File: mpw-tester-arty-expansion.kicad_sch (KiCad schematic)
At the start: 119 parts, among them J1 USB4105-GF-A, J10 61300211121, J11 61300211121, J12 61300211121, J14 61300311121, J15 61300311121, J18 61300411121, J19 61300711121, J2 61300211121, J20 61300411121, J3 Arty_A7_SPI, J4 61300211121, J5 61300311121, J6 61300211121, J7 61300211121, J8 61300211121, J9 61300211121, Q1 DTC014TEBTL, U1 SN74LVC1G125DCKR, U2 FT232HQ, U3 SN74LVC1G125DCKR, U4 MAX811REUS+T, U5 NTS0102DP, U6 MCP4661-103E/ML, U7 Caravel_breakout_PCB, U8 W25Q32FVSS, U9 MIC2211-AAYML-TR, Y1 ABM8G-12.000MHZ-18-D2Y-T, Y2 ECS-2520MVLC-100-BN-TR

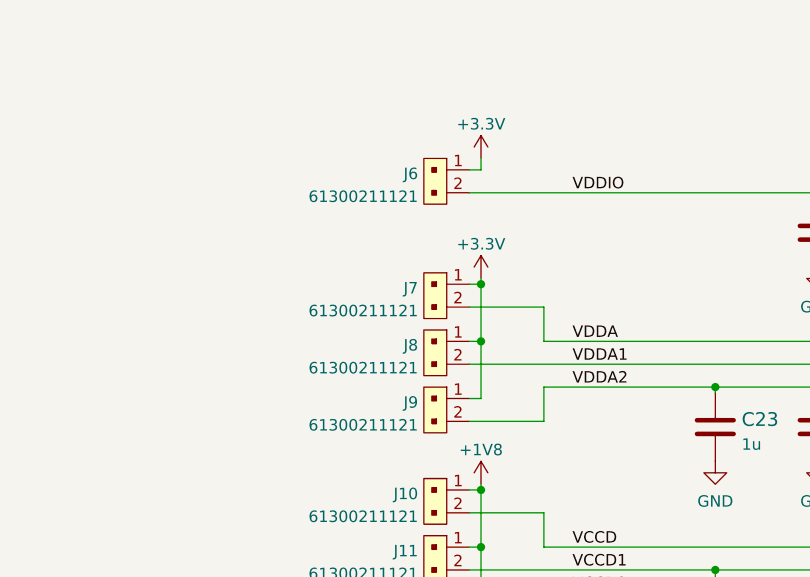
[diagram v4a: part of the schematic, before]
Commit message: Start power section layout. Adjust J6-J12 position on schematic to resolve crosses on PCB
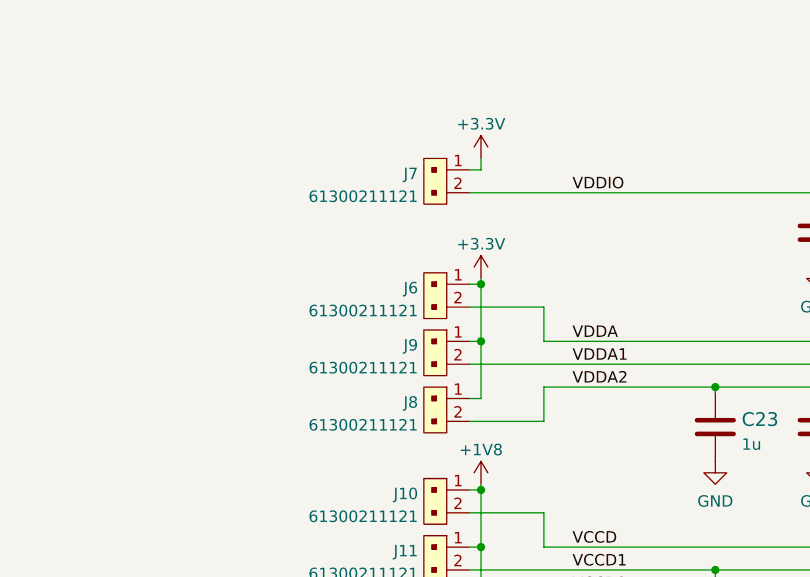
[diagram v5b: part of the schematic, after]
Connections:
- net VDDA: now also J6.2; no longer J7.2
- net VDDA1: now also J9.2; no longer J8.2
- net VDDA2: now also J8.2; no longer J9.2
- net VDDIO: now also J7.2; no longer J6.2
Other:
- moved on the sheet: J6, J7, J8, J9
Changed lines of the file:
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@@
     (rev "0.0.99")
   )
-  (bus_alias "SPI_FLASH" (members "~{CS}" "SCK" "SI" "SO" "~{WP}" "~{HOLD}"))
   (bus_alias "SPI" (members "~{CS}" "MISO" "MOSI" "SCK"))
+  (bus_alias "SPI_FLASH" (members "~{CS}" "SCK" "SI" "SO" "~{WP}" "~{HOLD}"))
   (junction (at 122.555 74.93) (diameter 0) (color 0 0 0 0)
   )
@@
     (pin "8")
   )
-  (symbol (lib_id "antmicroRectangularConnectorsHeadersMalePins:61300211121") (at 305.435 182.245 270) (unit 1)
+  (symbol (lib_id "antmicroRectangularConnectorsHeadersMalePins:61300211121") (at 305.435 169.545 270) (unit 1)
     (in_bom yes) (on_board yes) (fields_autoplaced)
-    (property "Reference" "J7" (id 0) (at 302.26 182.6803 90)
+    (property "Reference" "J7" (id 0) (at 302.26 169.9803 90)
       (effects (font (size 1.27 1.27)) (justify right))
     )
-    (property "Value" "61300211121" (id 1) (at 302.26 185.2172 90)
+    (property "Value" "61300211121" (id 1) (at 302.26 172.5172 90)
       (effects (font (size 1.27 1.27)) (justify right))
     )
-    (property "Footprint" "antmicro-footprints:PinHeader_1x2_P2.54_Drill0.9mm" (id 2) (at 310.515 187.325 0)
+    (property "Footprint" "antmicro-footprints:PinHeader_1x2_P2.54_Drill0.9mm" (id 2) (at 310.515 174.625 0)
       (effects (font (size 1.524 1.524)) (justify left) hide)
     )
-    (property "Datasheet" "https://katalog.we-online.de/em/datasheet/6130xx11121.pdf" (id 3) (at 313.055 187.325 0)
+    (property "Datasheet" "https://katalog.we-online.de/em/datasheet/6130xx11121.pdf" (id 3) (at 313.055 174.625 0)
       (effects (font (size 1.524 1.524)) (justify left) hide)
     )
-    (property "MPN" "61300211121" (id 4) (at 318.135 187.325 0)
+    (property "MPN" "61300211121" (id 4) (at 318.135 174.625 0)
       (effects (font (size 1.524 1.524)) (justify left) hide)
     )
-    (property "Manufacturer" "Wurth Electronic" (id 5) (at 333.375 187.325 0)
+    (property "Manufacturer" "Wurth Electronic" (id 5) (at 333.375 174.625 0)
       (effects (font (size 1.524 1.524)) (justify left) hide)
     )
@@
     (pin "2")
   )
-  (symbol (lib_id "antmicroRectangularConnectorsHeadersMalePins:61300211121") (at 305.435 169.545 270) (unit 1)
+  (symbol (lib_id "antmicroRectangularConnectorsHeadersMalePins:61300211121") (at 305.435 182.245 270) (unit 1)
     (in_bom yes) (on_board yes) (fields_autoplaced)
-    (property "Reference" "J6" (id 0) (at 302.26 169.9803 90)
+    (property "Reference" "J6" (id 0) (at 302.26 182.6803 90)
       (effects (font (size 1.27 1.27)) (justify right))
     )
-    (property "Value" "61300211121" (id 1) (at 302.26 172.5172 90)
+    (property "Value" "61300211121" (id 1) (at 302.26 185.2172 90)
       (effects (font (size 1.27 1.27)) (justify right))
     )
-    (property "Footprint" "antmicro-footprints:PinHeader_1x2_P2.54_Drill0.9mm" (id 2) (at 310.515 174.625 0)
+    (property "Footprint" "antmicro-footprints:PinHeader_1x2_P2.54_Drill0.9mm" (id 2) (at 310.515 187.325 0)
       (effects (font (size 1.524 1.524)) (justify left) hide)
     )
-    (property "Datasheet" "https://katalog.we-online.de/em/datasheet/6130xx11121.pdf" (id 3) (at 313.055 174.625 0)
+    (property "Datasheet" "https://katalog.we-online.de/em/datasheet/6130xx11121.pdf" (id 3) (at 313.055 187.325 0)
       (effects (font (size 1.524 1.524)) (justify left) hide)
     )
-    (property "MPN" "61300211121" (id 4) (at 318.135 174.625 0)
+    (property "MPN" "61300211121" (id 4) (at 318.135 187.325 0)
       (effects (font (size 1.524 1.524)) (justify left) hide)
     )
-    (property "Manufacturer" "Wurth Electronic" (id 5) (at 333.375 174.625 0)
+    (property "Manufacturer" "Wurth Electronic" (id 5) (at 333.375 187.325 0)
       (effects (font (size 1.524 1.524)) (justify left) hide)
     )
@@
     (pin "2")
   )
-  (symbol (lib_id "antmicroRectangularConnectorsHeadersMalePins:61300211121") (at 305.435 188.595 270) (unit 1)
+  (symbol (lib_id "antmicroRectangularConnectorsHeadersMalePins:61300211121") (at 305.435 194.945 270) (unit 1)
     (in_bom yes) (on_board yes) (fields_autoplaced)
-    (property "Reference" "J8" (id 0) (at 302.26 189.0303 90)
+    (property "Reference" "J8" (id 0) (at 302.26 195.3803 90)
       (effects (font (size 1.27 1.27)) (justify right))
     )
-    (property "Value" "61300211121" (id 1) (at 302.26 191.5672 90)
+    (property "Value" "61300211121" (id 1) (at 302.26 197.9172 90)
       (effects (font (size 1.27 1.27)) (justify right))
     )
-    (property "Footprint" "antmicro-footprints:PinHeader_1x2_P2.54_Drill0.9mm" (id 2) (at 310.515 193.675 0)
+    (property "Footprint" "antmicro-footprints:PinHeader_1x2_P2.54_Drill0.9mm" (id 2) (at 310.515 200.025 0)
       (effects (font (size 1.524 1.524)) (justify left) hide)
     )
-    (property "Datasheet" "https://katalog.we-online.de/em/datasheet/6130xx11121.pdf" (id 3) (at 313.055 193.675 0)
+    (property "Datasheet" "https://katalog.we-online.de/em/datasheet/6130xx11121.pdf" (id 3) (at 313.055 200.025 0)
       (effects (font (size 1.524 1.524)) (justify left) hide)
     )
-    (property "MPN" "61300211121" (id 4) (at 318.135 193.675 0)
+    (property "MPN" "61300211121" (id 4) (at 318.135 200.025 0)
       (effects (font (size 1.524 1.524)) (justify left) hide)
     )
-    (property "Manufacturer" "Wurth Electronic" (id 5) (at 333.375 193.675 0)
+    (property "Manufacturer" "Wurth Electronic" (id 5) (at 333.375 200.025 0)
       (effects (font (size 1.524 1.524)) (justify left) hide)
     )
@@
     (pin "2")
   )
-  (symbol (lib_id "antmicroRectangularConnectorsHeadersMalePins:61300211121") (at 305.435 194.945 270) (unit 1)
+  (symbol (lib_id "antmicroRectangularConnectorsHeadersMalePins:61300211121") (at 305.435 188.595 270) (unit 1)
     (in_bom yes) (on_board yes) (fields_autoplaced)
-    (property "Reference" "J9" (id 0) (at 302.26 195.3803 90)
+    (property "Reference" "J9" (id 0) (at 302.26 189.0303 90)
       (effects (font (size 1.27 1.27)) (justify right))
     )
-    (property "Value" "61300211121" (id 1) (at 302.26 197.9172 90)
+    (property "Value" "61300211121" (id 1) (at 302.26 191.5672 90)
       (effects (font (size 1.27 1.27)) (justify right))
     )
-    (property "Footprint" "antmicro-footprints:PinHeader_1x2_P2.54_Drill0.9mm" (id 2) (at 310.515 200.025 0)
+    (property "Footprint" "antmicro-footprints:PinHeader_1x2_P2.54_Drill0.9mm" (id 2) (at 310.515 193.675 0)
       (effects (font (size 1.524 1.524)) (justify left) hide)
     )
-    (property "Datasheet" "https://katalog.we-online.de/em/datasheet/6130xx11121.pdf" (id 3) (at 313.055 200.025 0)
+    (property "Datasheet" "https://katalog.we-online.de/em/datasheet/6130xx11121.pdf" (id 3) (at 313.055 193.675 0)
       (effects (font (size 1.524 1.524)) (justify left) hide)
     )
-    (property "MPN" "61300211121" (id 4) (at 318.135 200.025 0)
+    (property "MPN" "61300211121" (id 4) (at 318.135 193.675 0)
       (effects (font (size 1.524 1.524)) (justify left) hide)
     )
-    (property "Manufacturer" "Wurth Electronic" (id 5) (at 333.375 200.025 0)
+    (property "Manufacturer" "Wurth Electronic" (id 5) (at 333.375 193.675 0)
       (effects (font (size 1.524 1.524)) (justify left) hide)
     )

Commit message: Change page size to A3, add diodes to buffer UART_EN and MR signals
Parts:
- removed D5, D6: 1N5819HW-7-F, antmicro-footprints:SOD-123, symbol antmicroDiodesRectifiersSingle:1N5819HW-7-F
- removed NT1, NT10, NT11, NT12, NT2, NT3, NT4, NT5, NT6, NT7, NT8, NT9: NetTie_2, antmicro-footprints:NetTie-2_SMD_Pad0.127mm, symbol antmicroShuntsJumpers:NetTie_2
- added D5, D6, D9: PMEG6002EJ,115, antmicro-footprints:SOD-323F, symbol antmicroDiodesRectifiersSingle:PMEG6002EJ,115
- added D7, D8: 1N5819HW-7-F, antmicro-footprints:SOD-123, symbol antmicroDiodesRectifiersSingle:1N5819HW-7-F
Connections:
- net ARTY_CS is gone; now on net CRVL_IO3: J3.52 (IO12)
- net ARTY_MISO is gone; now on net CRVL_IO1: J3.51 (IO13)
- net ARTY_MOSI is gone; now on net CRVL_IO2: J3.34 (IO38)
- net ARTY_RX is gone; now on net CRVL_IO6: J3.36 (IO36)
- net ARTY_SCK is gone; now on net CRVL_IO4: J3.35 (IO37)
- net ARTY_TX is gone; now on net CRVL_IO5: J3.53 (IO11)
- net CRVL_RX is gone; now on net CRVL_IO6: J18.3
- net CRVL_TX is gone; now on net CRVL_IO5: J18.2
- net GPIO is gone; now on net CRVL_GPIO: Q1.1 (B)
- net USB_CS1 is gone; now on net CRVL_IO3: U2.16 (ADBUS3)
- net USB_SI is gone; now on net CRVL_IO1: U2.15 (ADBUS2)
- net 5V0: now also D7.K, D8.K
- net 5V0_ARTY: now also D8.A
- net CRVL_IO2: now also U2.14 (ADBUS1)
- net CRVL_IO4: now also U2.13 (ADBUS0)
- net EN_VOUT1: now also J3.19 (A6); no longer J3.9 (A0)
- net EN_VOUT2: now also J3.9 (A0); no longer J3.19 (A6)
- net USB_SCK_TXD: no longer U2.13 (ADBUS0)
- net USB_SO_RXD: no longer U2.14 (ADBUS1)
- net VBUS: now also D7.A
- net ~{MR}: now also D6.A, D9.A; no longer J3.31 (IO41), U2.25 (ACBUS1)
- net ~{UART_EN}: now also D5.A; no longer U2.21 (ACBUS0)
- new net: D5.K, U2.21 (ACBUS0)
- new net: D6.K, U2.25 (ACBUS1)
- new net: D9.K, J3.31 (IO41)
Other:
- note added: "ARTY_RX"
- note added: "ARTY_TX"
- note added: "CRVL_RX"
- note added: "CRVL_TX"
- note added: "CS1"
- note added: "MISO"
- note added: "MISO / RXD"
- note added: "MOSI"
- note added: "POWER LED"
- note added: "SCK"
- note added: "SCK / TXD"
- note added: "USR LED"
- note removed: "Dynamic Power Supplies"
- note removed: "FTDI interface with HKSPI"
- note removed: "LED, test points"
- moved on the sheet: C1, C10, C11, C12, C14, C15, C16, C17, C18, C19, C2, C20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

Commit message: Fix label names
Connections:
- net USB_SCK_TXD is gone; now on net ADBUS0: U1.2 (A)
- net USB_SO_RXD is gone; now on net ADBUS1: U3.4 (Y)
- net CRVL_IO1 renamed ADBUS2
- net CRVL_IO2 renamed ADBUS1
- net CRVL_IO3 renamed ADBUS3
- net CRVL_IO4 renamed ADBUS0
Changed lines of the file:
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@@
     (stroke (width 0) (type default) (color 0 0 0 0))
   )
-  (bus_entry (at 147.32 24.765) (size -2.54 2.54)
+  (bus_entry (at 153.67 24.765) (size -2.54 2.54)
     (stroke (width 0) (type default) (color 0 0 0 0))
   )
@@
     (stroke (width 0) (type default) (color 0 0 0 0))
   )
-  (bus_entry (at 147.32 29.845) (size -2.54 2.54)
+  (bus_entry (at 153.67 29.845) (size -2.54 2.54)
     (stroke (width 0) (type default) (color 0 0 0 0))
   )
@@
     (stroke (width 0) (type default) (color 0 0 0 0))
   )
-  (bus_entry (at 147.32 29.845) (size -2.54 2.54)
+  (bus_entry (at 153.67 29.845) (size -2.54 2.54)
     (stroke (width 0) (type default) (color 0 0 0 0))
   )
@@
     (stroke (width 0) (type default) (color 0 0 0 0))
   )
-  (bus_entry (at 147.32 22.225) (size -2.54 2.54)
-    (stroke (width 0) (type default) (color 0 0 0 0))
-  )
-  (bus_entry (at 147.32 24.765) (size -2.54 2.54)
+  (bus_entry (at 153.67 22.225) (size -2.54 2.54)
+    (stroke (width 0) (type default) (color 0 0 0 0))
+  )
+  (bus_entry (at 153.67 24.765) (size -2.54 2.54)
     (stroke (width 0) (type default) (color 0 0 0 0))
   )
@@
     (stroke (width 0) (type default) (color 0 0 0 0))
   )
-  (bus_entry (at 147.32 27.305) (size -2.54 2.54)
+  (bus_entry (at 153.67 27.305) (size -2.54 2.54)
     (stroke (width 0) (type default) (color 0 0 0 0))
   )
@@
     (stroke (width 0) (type default) (color 0 0 0 0))
   )
-  (bus_entry (at 147.32 27.305) (size -2.54 2.54)
+  (bus_entry (at 153.67 27.305) (size -2.54 2.54)
     (stroke (width 0) (type default) (color 0 0 0 0))
   )
@@
     (stroke (width 0) (type default) (color 0 0 0 0))
   )
-  (bus (pts (xy 148.59 20.32) (xy 147.32 21.59))
+  (bus (pts (xy 154.94 20.32) (xy 153.67 21.59))
     (stroke (width 0) (type default) (color 0 0 0 0))
   )
@@
     (stroke (width 0) (type default) (color 0 0 0 0))
   )
-  (bus (pts (xy 147.32 22.225) (xy 147.32 24.765))
+  (bus (pts (xy 153.67 22.225) (xy 153.67 24.765))
     (stroke (width 0) (type default) (color 0 0 0 0))
   )
@@
     (stroke (width 0) (type default) (color 0 0 0 0))
   )
+  (wire (pts (xy 130.81 24.765) (xy 151.13 24.765))
+    (stroke (width 0) (type default) (color 0 0 0 0))
+  )
   (wire (pts (xy 72.39 100.965) (xy 72.39 103.505))
     (stroke (width 0) (type default) (color 0 0 0 0))
@@
     (stroke (width 0) (type default) (color 0 0 0 0))
   )
-  (wire (pts (xy 130.81 32.385) (xy 144.78 32.385))
-    (stroke (width 0) (type default) (color 0 0 0 0))
-  )
   (wire (pts (xy 163.195 51.435) (xy 163.195 52.07))
     (stroke (width 0) (type default) (color 0 0 0 0))
@@
     (stroke (width 0) (type default) (color 0 0 0 0))
   )
-  (wire (pts (xy 130.81 29.845) (xy 144.78 29.845))
+  (wire (pts (xy 130.81 29.845) (xy 151.13 29.845))
     (stroke (width 0) (type default) (color 0 0 0 0))
   )
@@
     (stroke (width 0) (type default) (color 0 0 0 0))
   )
+  (wire (pts (xy 130.81 32.385) (xy 151.13 32.385))
+    (stroke (width 0) (type default) (color 0 0 0 0))
+  )
   (wire (pts (xy 226.695 172.72) (xy 245.11 172.72))
     (stroke (width 0) (type default) (color 0 0 0 0))
@@
     (stroke (width 0) (type default) (color 0 0 0 0))
   )
+  (wire (pts (xy 130.81 27.305) (xy 151.13 27.305))
+    (stroke (width 0) (type default) (color 0 0 0 0))
+  )
   (wire (pts (xy 48.895 71.755) (xy 48.895 73.025))
     (stroke (width 0) (type default) (color 0 0 0 0))
@@
     (stroke (width 0) (type default) (color 0 0 0 0))
   )
-  (bus (pts (xy 147.32 24.765) (xy 147.32 27.305))
+  (bus (pts (xy 153.67 24.765) (xy 153.67 27.305))
     (stroke (width 0) (type default) (color 0 0 0 0))
   )
@@
     (stroke (width 0) (type default) (color 0 0 0 0))
   )
-  (bus (pts (xy 164.465 20.32) (xy 148.59 20.32))
+  (bus (pts (xy 170.815 20.32) (xy 154.94 20.32))
     (stroke (width 0) (type default) (color 0 0 0 0))
   )
@@
     (stroke (width 0) (type default) (color 0 0 0 0))
   )
-  (bus (pts (xy 147.32 21.59) (xy 147.32 22.225))
+  (bus (pts (xy 153.67 21.59) (xy 153.67 22.225))
     (stroke (width 0) (type default) (color 0 0 0 0))
   )
@@
     (stroke (width 0) (type default) (color 0 0 0 0))
   )
-  (wire (pts (xy 130.81 27.305) (xy 144.78 27.305))
-    (stroke (width 0) (type default) (color 0 0 0 0))
-  )
   (bus (pts (xy 153.035 216.535) (xy 153.035 219.075))
     (stroke (width 0) (type default) (color 0 0 0 0))
@@
     (stroke (width 0) (type default) (color 0 0 0 0))
   )
-  (wire (pts (xy 130.81 24.765) (xy 144.78 24.765))
-    (stroke (width 0) (type default) (color 0 0 0 0))
-  )
   (wire (pts (xy 102.235 50.165) (xy 102.235 52.705))
     (stroke (width 0) (type default) (color 0 0 0 0))
@@
     (stroke (width 0) (type default) (color 0 0 0 0))
   )
-  (bus (pts (xy 147.32 27.305) (xy 147.32 29.845))
+  (bus (pts (xy 153.67 27.305) (xy 153.67 29.845))
     (stroke (width 0) (type default) (color 0 0 0 0))
   )
@@
     (effects (font (size 1.27 1.27)) (justify left bottom))
   )
-  (text "SCK  / TXD" (at 149.86 24.765 0)
+  (text "SCK  / TXD" (at 156.21 24.765 0)
     (effects (font (size 1.27 1.27)) (justify left bottom))
   )
@@
     (effects (font (size 1.5 1.5) (thickness 0.3) bold) (justify left bottom))
   )
-  (text "MISO / RXD" (at 149.86 27.305 0)
+  (text "MISO / RXD" (at 156.21 27.305 0)
     (effects (font (size 1.27 1.27)) (justify left bottom))
   )
@@
     (effects (font (size 2 2) (thickness 0.4) bold) (justify left bottom))
   )
-  (text "MOSI" (at 149.86 29.845 0)
-    (effects (font (size 1.27 1.27)) (justify left bottom))
-  )
-  (text "CS1" (at 149.86 32.385 0)
+  (text "MOSI" (at 156.21 29.845 0)
+    (effects (font (size 1.27 1.27)) (justify left bottom))
+  )
+  (text "CS1" (at 156.21 32.385 0)
     (effects (font (size 1.27 1.27)) (justify left bottom))
   )
@@
     (effects (font (size 1.27 1.27)) (justify left bottom))
   )
+  (label "ADBUS2" (at 131.445 29.845 0)
+    (effects (font (size 1.27 1.27)) (justify left bottom))
+  )
   (label "XOUT" (at 96.52 98.425 0)
     (effects (font (size 1.27 1.27)) (justify left bottom))
@@
     (effects (font (size 1.27 1.27)) (justify left bottom))
   )
-  (label "CRVL_IO4" (at 144.78 24.765 180)
+  (label "CRVL_IO4" (at 151.13 24.765 180)
     (effects (font (size 1.27 1.27)) (justify right bottom))
   )
@@
     (effects (font (size 1.27 1.27)) (justify left bottom))
   )
+  (label "ADBUS3" (at 131.445 32.385 0)
+    (effects (font (size 1.27 1.27)) (justify left bottom))
+  )
   (label "CRVL_IO2" (at 138.43 147.955 0)
     (effects (font (size 1.27 1.27)) (justify left bottom))
@@
     (effects (font (size 1.27 1.27)) (justify right bottom))
   )
-  (label "CRVL_IO2" (at 144.78 27.305 180)
+  (label "CRVL_IO2" (at 151.13 27.305 180)
     (effects (font (size 1.27 1.27)) (justify right bottom))
   )
@@
     (effects (font (size 1.27 1.27)) (justify left bottom))
   )
+  (label "ADBUS0" (at 203.2 55.88 0)
+    (effects (font (size 1.27 1.27)) (justify left bottom))
+  )
   (label "CRVL_IO18" (at 138.43 188.595 0)
     (effects (font (size 1.27 1.27)) (justify left bottom))
@@
   (label "~{TX_LED}" (at 144.78 62.865 180)
     (effects (font (size 1.27 1.27)) (justify right bottom))
+  )
+  (label "ADBUS0" (at 131.445 24.765 0)
+    (effects (font (size 1.27 1.27)) (justify left bottom))
   )
   (label "CRVL_IO32" (at 323.85 191.135 180)
@@
     (effects (font (size 1 1)) (justify left bottom))
   )
+  (label "ADBUS1" (at 244.475 100.33 180)
+    (effects (font (size 1.27 1.27)) (justify right bottom))
+  )
   (label "FTDI_3V3" (at 59.055 67.945 0)
     (effects (font (size 1.27 1.27)) (justify left bottom))
@@
     (effects (font (size 1.27 1.27)) (justify left bottom))
   )
-  (label "CRVL_IO3" (at 144.78 32.385 180)
+  (label "CRVL_IO3" (at 151.13 32.385 180)
     (effects (font (size 1.27 1.27)) (justify right bottom))
   )
@@
     (effects (font (size 1.27 1.27)) (justify right bottom))
   )
-  (label "USB_SO_RXD" (at 244.475 100.33 180)
-    (effects (font (size 1.27 1.27)) (justify right bottom))
-  )
   (label "ARTY_XCLK" (at 53.975 208.915 180)
     (effects (font (size 1.27 1.27)) (justify right bottom))
@@
     (effects (font (size 1.27 1.27)) (justify right bottom))
   )
-  (label "CRVL_IO[0..37]" (at 164.465 20.32 180)
+  (label "CRVL_IO[0..37]" (at 170.815 20.32 180)
     (effects (font (size 1.27 1.27)) (justify right bottom))
   )
@@
     (effects (font (size 1.27 1.27)) (justify left bottom))
   )
+  (label "ADBUS1" (at 131.445 27.305 0)
+    (effects (font (size 1.27 1.27)) (justify left bottom))
+  )
   (label "VDDIO" (at 227.33 147.32 0)
     (effects (font (size 1.27 1.27)) (justify left bottom))
@@
     (effects (font (size 1.27 1.27)) (justify left bottom))
   )
-  (label "CRVL_IO1" (at 144.78 29.845 180)
+  (label "CRVL_IO1" (at 151.13 29.845 180)
     (effects (font (size 1.27 1.27)) (justify right bottom))
   )
@@
     (effects (font (size 1.27 1.27)) (justify right bottom))
   )
-  (label "USB_SCK_TXD" (at 203.2 55.88 0)
-    (effects (font (size 1.27 1.27)) (justify left bottom))
-  )
   (label "CRVL_IO34" (at 138.43 229.235 0)
